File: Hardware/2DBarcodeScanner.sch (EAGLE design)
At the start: 36 parts, among them Q1 600mA/40V, Q2 600mA/40V, U1 3.3V, U2 BARCODE_SCANNER_MOUNT

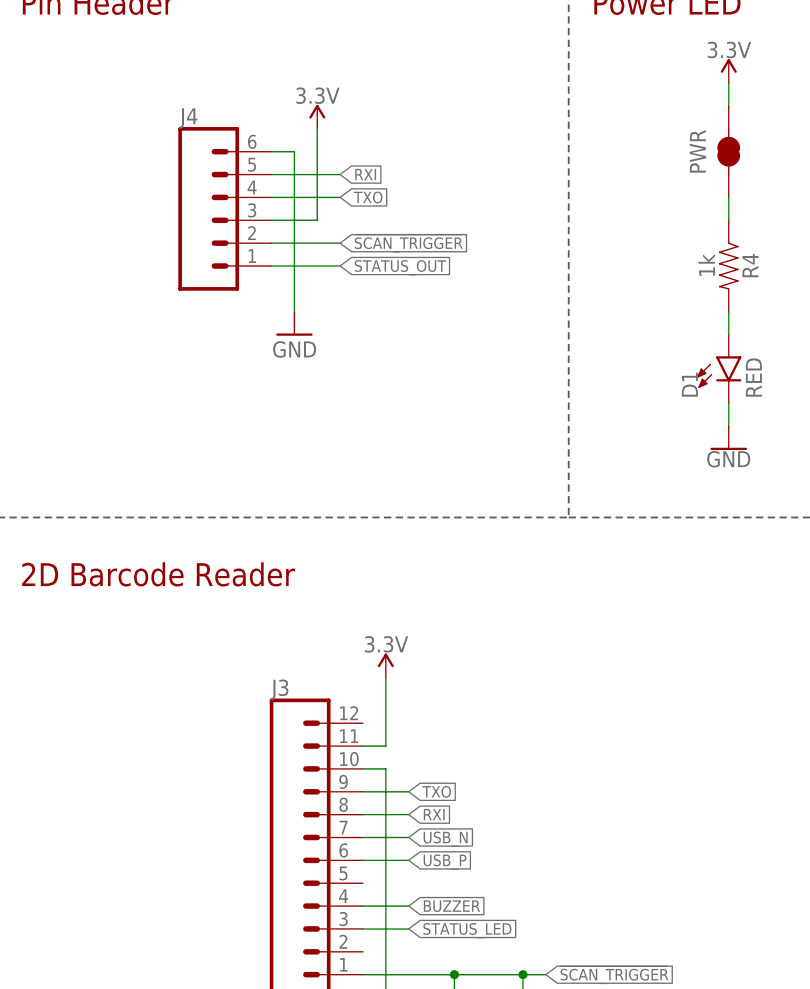
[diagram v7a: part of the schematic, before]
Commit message: Flip TX and RX pins
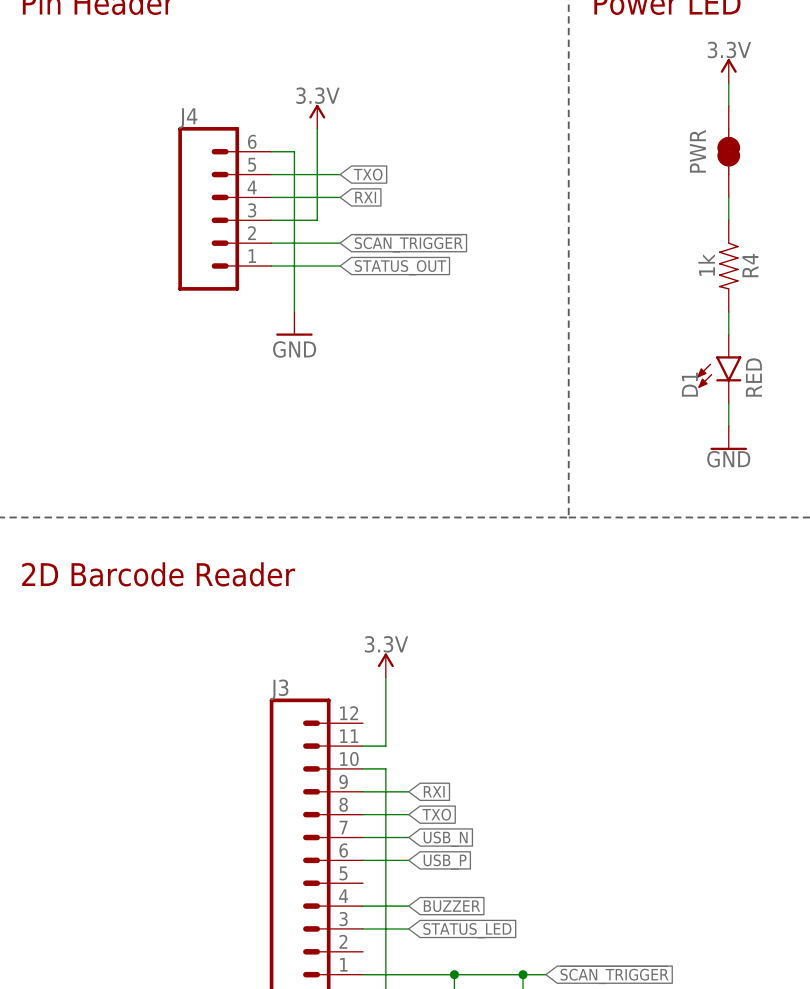
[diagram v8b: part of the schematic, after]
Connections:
- net RXI: now also J3.9, J4.4; no longer J3.8, J4.5
- net TXO: now also J3.8, J4.5; no longer J3.9, J4.4
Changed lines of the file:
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@@
 <net name="TXO" class="0">
+<segment>
+<pinref part="J3" gate="G$1" pin="8"/>
+<wire x1="190.5" y1="88.9" x2="195.58" y2="88.9" width="0.1524" layer="91"/>
+<label x="195.58" y="88.9" size="1.27" layer="95" xref="yes"/>
+</segment>
+<segment>
+<pinref part="J4" gate="G$1" pin="5"/>
+<wire x1="180.34" y1="160.02" x2="187.96" y2="160.02" width="0.1524" layer="91"/>
+<label x="187.96" y="160.02" size="1.27" layer="95" xref="yes"/>
+</segment>
+</net>
+<net name="RXI" class="0">
+<segment>
+<pinref part="J3" gate="G$1" pin="9"/>
+<wire x1="190.5" y1="91.44" x2="195.58" y2="91.44" width="0.1524" layer="91"/>
+<label x="195.58" y="91.44" size="1.27" layer="95" xref="yes"/>
+</segment>
 <segment>
 <pinref part="J4" gate="G$1" pin="4"/>
@@
 <label x="187.96" y="157.48" size="1.27" layer="95" xref="yes"/>
 </segment>
-<segment>
-<pinref part="J3" gate="G$1" pin="9"/>
-<wire x1="190.5" y1="91.44" x2="195.58" y2="91.44" width="0.1524" layer="91"/>
-<label x="195.58" y="91.44" size="1.27" layer="95" xref="yes"/>
-</segment>
 </net>
-<net name="RXI" class="0">
-<segment>
-<pinref part="J4" gate="G$1" pin="5"/>
-<wire x1="180.34" y1="160.02" x2="187.96" y2="160.02" width="0.1524" layer="91"/>
-<label x="187.96" y="160.02" size="1.27" layer="95" xref="yes"/>
-</segment>
-<segment>
-<pinref part="J3" gate="G$1" pin="8"/>
-<wire x1="190.5" y1="88.9" x2="195.58" y2="88.9" width="0.1524" layer="91"/>
-<label x="195.58" y="88.9" size="1.27" layer="95" xref="yes"/>
-</segment>
-</net>
